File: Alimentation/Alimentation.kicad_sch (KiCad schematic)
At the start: 8 parts, among them J1 RPI, J2 STEPPER, J3 LORA, J4 BATTERY RPI EXPE, J5 BATTERY LORA, J6 RPI_VOUT, J7 STEPPER_VOUT, J8 LORA_VOUT

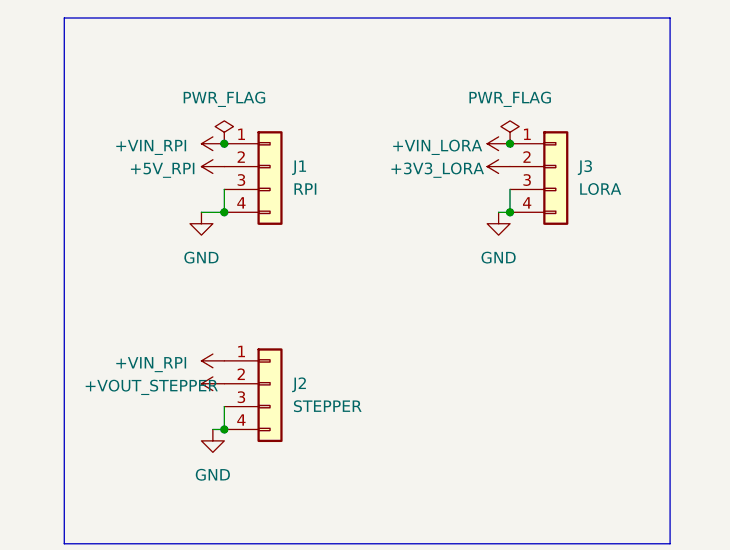
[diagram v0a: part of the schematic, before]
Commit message: Routed Power Board
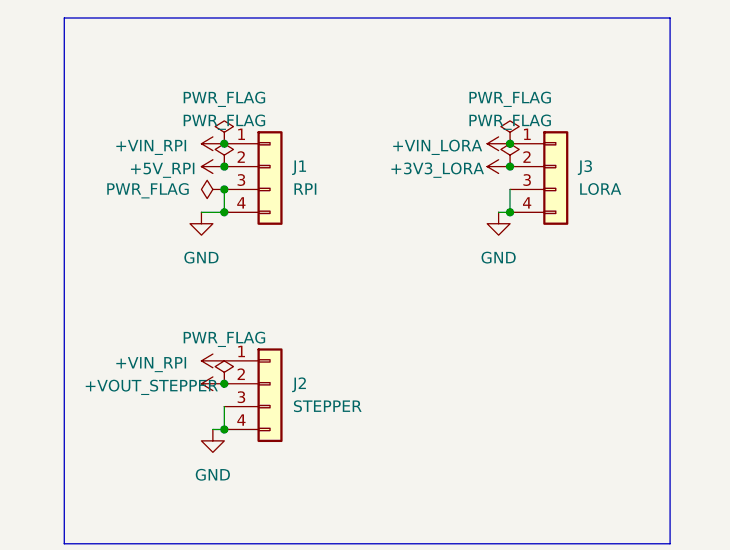
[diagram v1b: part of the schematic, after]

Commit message: Fully Routed Sensor board
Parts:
- added H1, H2, H3, H4: MountingHole_Pad, MountingHole:MountingHole_3.2mm_M3_DIN965_Pad, symbol Mechanical:MountingHole_Pad
- added J10: BATTERY PARACHUTE, PHOENIX_CON:AMASS_XT60-M_1x02_P7.20mm_Vertical, symbol Connector_Generic:Conn_01x02
- added J11: STEPPER_VOUT, Connector_JST:JST_XH_S4B-XH-A-1_1x04_P2.50mm_Horizontal, symbol Connector_Generic:Conn_01x04
- added J9: PARACHUTE, PHOENIX:BUCK_STEPDOWN_LM2592, symbol Connector_Generic:Conn_01x04
- J1, J2, J3: footprint PHOENIX:MT3608 -> PHOENIX:BUCK_STEPDOWN_LM2592
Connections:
- net GND: now also H1.1, H2.1, H3.1, H4.1, J10.2 (Pin_2), J11.3 (Pin_3), J11.4 (Pin_4), J9.3 (Pin_3), J9.4 (Pin_4)
- new net +5V_PARA: J11.1 (Pin_1), J11.2 (Pin_2), J9.2 (Pin_2)
- new net +VIN_PARA: J10.1 (Pin_1), J9.1 (Pin_1)
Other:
- note added: "Batteries for the expe lora rpi TIMER"
- note removed: "Batteries for the expe lora and rpi"

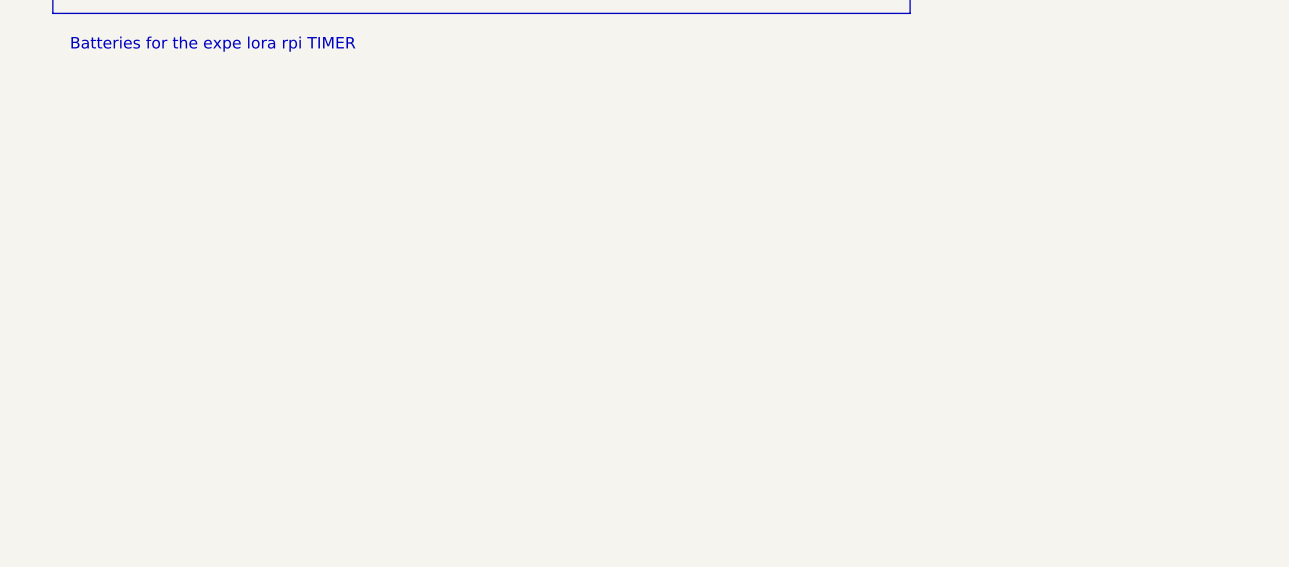
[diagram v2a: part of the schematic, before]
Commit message: flipped connections for the GPS connector to 3_3,RX <-> GND,TX
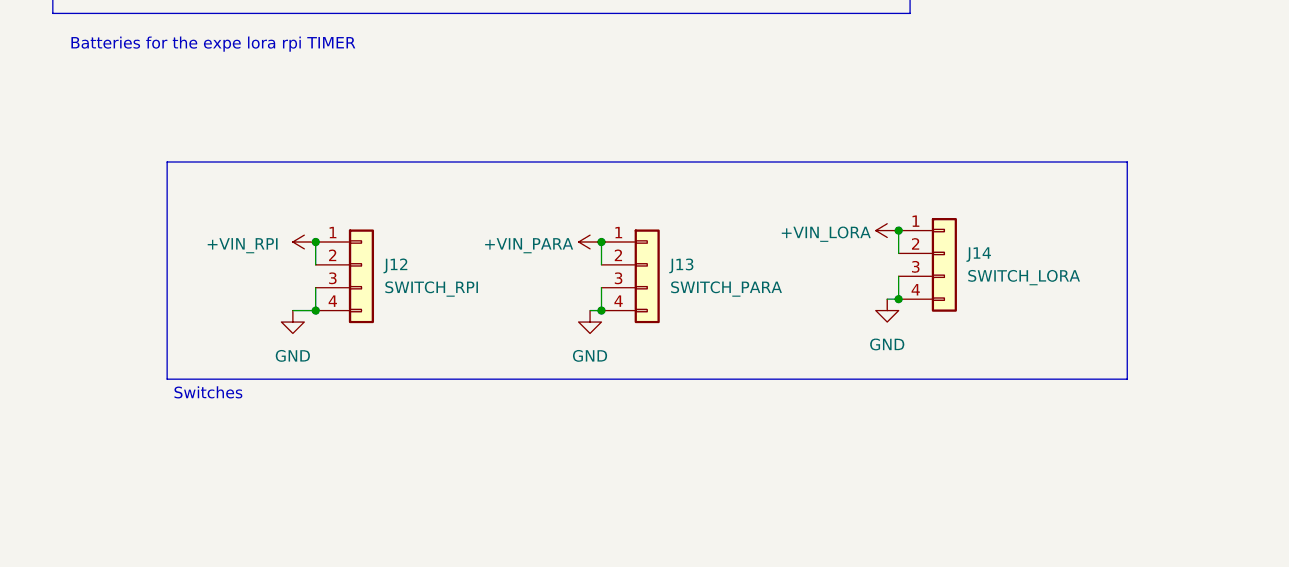
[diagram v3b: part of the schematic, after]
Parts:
- added J12: SWITCH_RPI, Connector_JST:JST_XH_S4B-XH-A-1_1x04_P2.50mm_Horizontal, symbol Connector_Generic:Conn_01x04
- added J13: SWITCH_PARA, Connector_JST:JST_XH_S4B-XH-A-1_1x04_P2.50mm_Horizontal, symbol Connector_Generic:Conn_01x04
- added J14: SWITCH_LORA, Connector_JST:JST_XH_S4B-XH-A-1_1x04_P2.50mm_Horizontal, symbol Connector_Generic:Conn_01x04
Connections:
- net +VIN_LORA: now also J14.1 (Pin_1), J14.2 (Pin_2)
- net +VIN_PARA: now also J13.1 (Pin_1), J13.2 (Pin_2)
- net +VIN_RPI: now also J12.1 (Pin_1), J12.2 (Pin_2)
- net GND: now also J12.3 (Pin_3), J12.4 (Pin_4), J13.3 (Pin_3), J13.4 (Pin_4), J14.3 (Pin_3), J14.4 (Pin_4)
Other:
- note added: "Switches"

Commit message: alimentation: full revision
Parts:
- removed H1, H2, H3, H4: MountingHole_Pad, MountingHole:MountingHole_3.2mm_M3_DIN965_Pad, symbol Mechanical:MountingHole_Pad
- J1, J2, J3, J9: footprint PHOENIX:BUCK_STEPDOWN_LM2592 -> nasa:LM2596
- J10, J4, J5: footprint PHOENIX_CON:AMASS_XT60-M_1x02_P7.20mm_Vertical -> Connector_AMASS:AMASS_XT60PW-M_1x02_P7.20mm_Horizontal
- J11: value STEPPER_VOUT -> PARACHUTE_VOUT; footprint Connector_JST:JST_XH_S4B-XH-A-1_1x04_P2.50mm_Horizontal -> Connector_JST:JST_XH_S4B-XH-A_1x04_P2.50mm_Horizontal
- J12, J13, J14: footprint Connector_JST:JST_XH_S4B-XH-A-1_1x04_P2.50mm_Horizontal -> Connector_JST:JST_XH_B4B-XH-A_1x04_P2.50mm_Vertical
- J6, J7, J8: footprint Connector_JST:JST_XH_S4B-XH-A-1_1x04_P2.50mm_Horizontal -> Connector_JST:JST_XH_S4B-XH-A_1x04_P2.50mm_Horizontal
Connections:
- net +VIN_LORA: no longer J3.1 (Pin_1)
- net +VIN_PARA: no longer J9.1 (Pin_1)
- net +VIN_RPI: no longer J1.1 (Pin_1), J2.1 (Pin_1)
- net GND: no longer J10.2 (Pin_2), J11.3 (Pin_3), J11.4 (Pin_4), J12.3 (Pin_3), J12.4 (Pin_4), J13.3 (Pin_3), J13.4 (Pin_4), J14.3 (Pin_3), J14.4 (Pin_4), J9.3 (Pin_3), J9.4 (Pin_4)
- new net +VCC_LORA: J14.3 (Pin_3), J14.4 (Pin_4), J3.1 (Pin_1)
- new net +VCC_PARA: J13.3 (Pin_3), J13.4 (Pin_4), J9.1 (Pin_1)
- new net +VCC_RPI: J1.1 (Pin_1), J12.3 (Pin_3), J12.4 (Pin_4), J2.1 (Pin_1)
- new net GND1: J10.2 (Pin_2), J11.3 (Pin_3), J11.4 (Pin_4), J9.3 (Pin_3), J9.4 (Pin_4)
